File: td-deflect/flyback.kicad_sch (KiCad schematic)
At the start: 50 parts, among them Q12 G3R450MT17J, U13 MCP1416

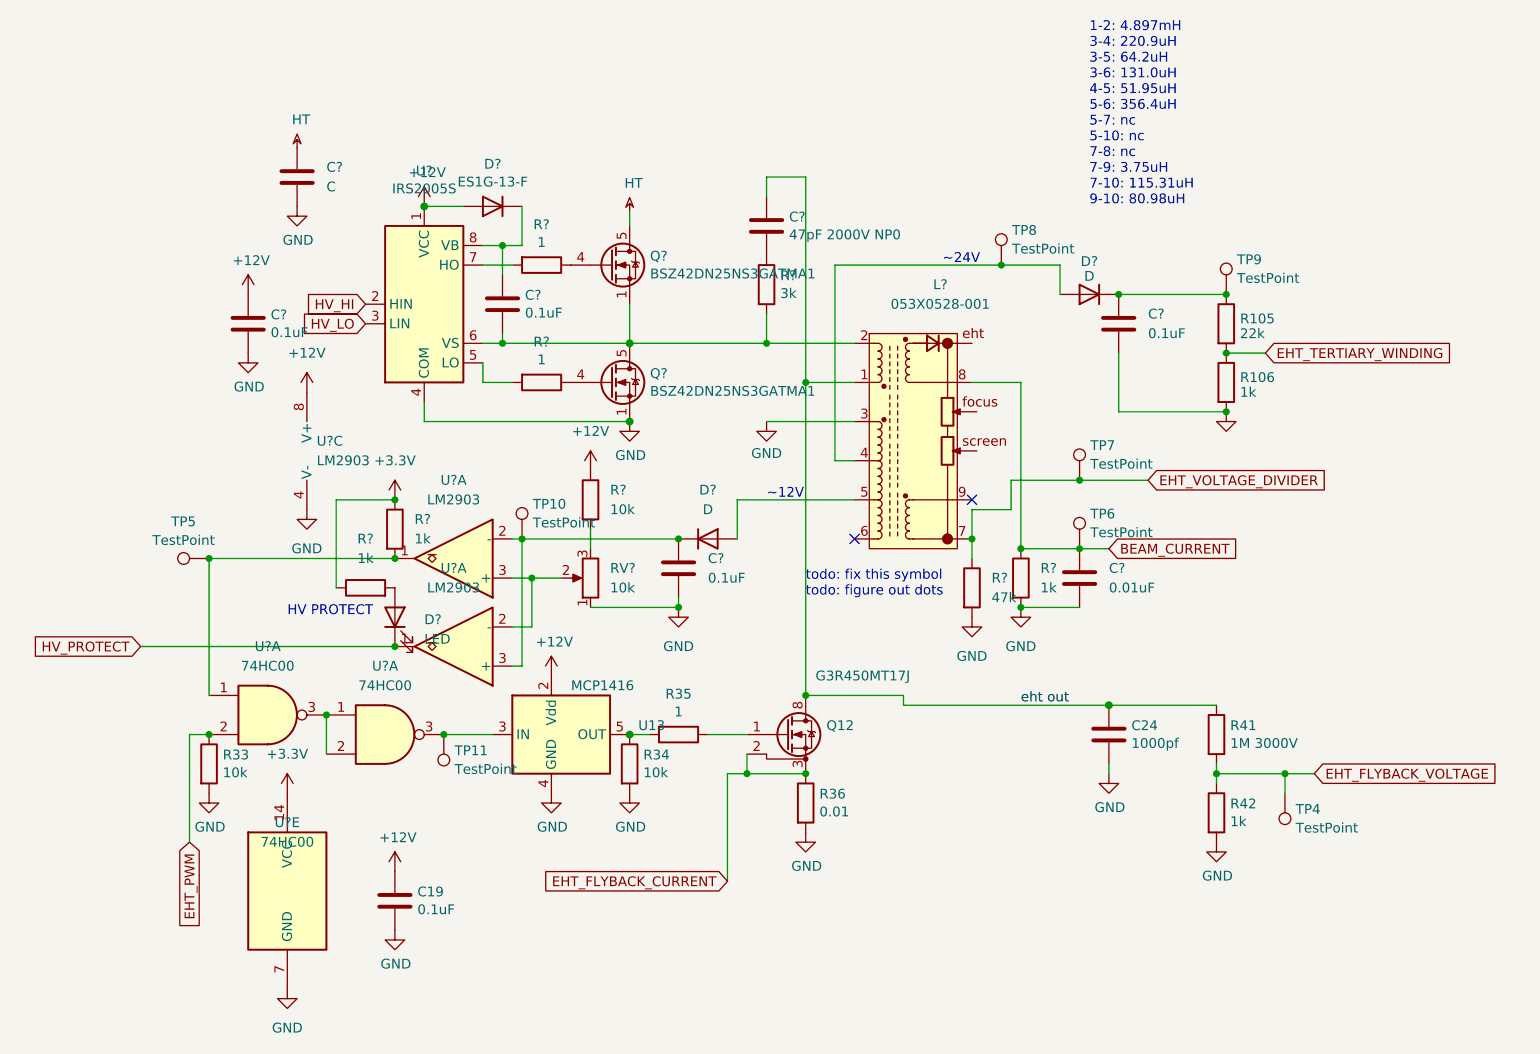
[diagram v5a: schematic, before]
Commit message: use offboard flyback
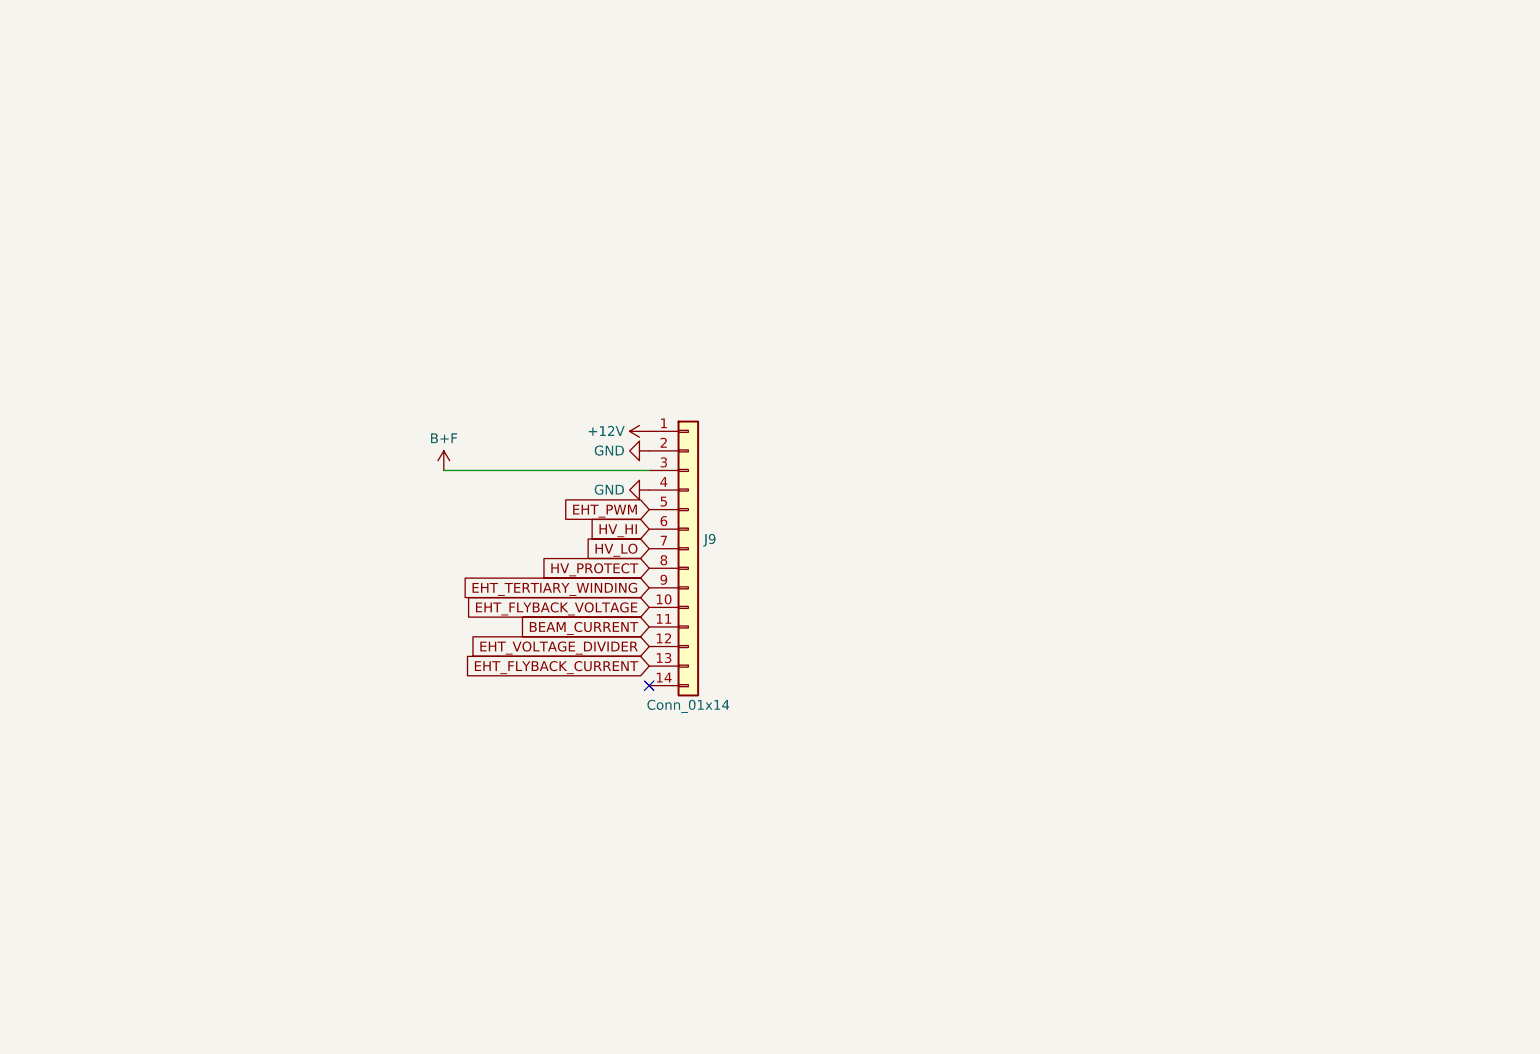
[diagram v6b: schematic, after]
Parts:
- removed C19, C? (x4): 0.1uF, Capacitor_SMD:C_0805_2012Metric_Pad1.18x1.45mm_HandSolder, symbol Device:C
- removed C24: 1000pf, Capacitor_THT:C_Rect_L18.0mm_W6.0mm_P15.00mm_FKS3_FKP3, symbol Device:C
- removed C?: 0.01uF, Capacitor_SMD:C_0805_2012Metric_Pad1.18x1.45mm_HandSolder, symbol Device:C
- removed C?: C, Capacitor_SMD:C_0805_2012Metric_Pad1.18x1.45mm_HandSolder, symbol Device:C
- removed C?: 47pF 2000V NP0, Capacitor_SMD:C_1206_3216Metric, symbol Device:C
- removed D? (x2): D, Diode_SMD:D_0805_2012Metric_Pad1.15x1.40mm_HandSolder, symbol Device:D
- removed D?: LED, Diode_SMD:D_0805_2012Metric_Pad1.15x1.40mm_HandSolder, symbol Device:LED
- removed D?: ES1G-13-F, Diode_SMD:D_SMA, symbol Diode:BA157
- removed L?: 053X0528-001, td-hv:053X0528-001, symbol td-hv:053X0528-001
- removed Q12: G3R450MT17J, Package_TO_SOT_SMD:TO-263-7_TabPin8, symbol Transistor_FET:C3M0280090J
- removed Q? (x2): BSZ42DN25NS3GATMA1, Package_TO_SOT_SMD:TDSON-8-1, symbol Transistor_FET:BSC082N10LSG
- removed R105: 22k, Resistor_SMD:R_0805_2012Metric_Pad1.20x1.40mm_HandSolder, symbol Device:R
- removed R106, R42, R? (x3): 1k, Resistor_SMD:R_0805_2012Metric_Pad1.20x1.40mm_HandSolder, symbol Device:R
- removed R33, R34, R?: 10k, Resistor_SMD:R_0805_2012Metric_Pad1.20x1.40mm_HandSolder, symbol Device:R
- removed R35, R? (x2): 1, Resistor_SMD:R_0805_2012Metric_Pad1.20x1.40mm_HandSolder, symbol Device:R
- removed R36: 0.01, Resistor_SMD:R_0805_2012Metric_Pad1.20x1.40mm_HandSolder, symbol Device:R
- removed R41: 1M 3000V, Resistor_SMD:R_2512_6332Metric, symbol Device:R
- removed R?: 47k, Resistor_SMD:R_0805_2012Metric_Pad1.20x1.40mm_HandSolder, symbol Device:R
- removed R?: 3k, Resistor_SMD:R_2512_6332Metric, symbol Device:R
- removed RV?: 10k, Potentiometer_THT:Potentiometer_Bourns_3386P_Vertical, symbol Device:R_Potentiometer
- removed TP10, TP11, TP4, TP5, TP6, TP7, TP8, TP9: TestPoint, TestPoint:TestPoint_Keystone_5010-5014_Multipurpose, symbol Connector:TestPoint
- removed U13: MCP1416, Package_TO_SOT_SMD:SOT-23-5, symbol Driver_FET:MCP1416
- removed U? (x3): LM2903, Package_SO:SOIC-8_3.9x4.9mm_P1.27mm, symbol Comparator:LM2903
- removed U? (x3): 74HC00, Package_SO:SOIC-14_3.9x8.7mm_P1.27mm, symbol 74xx:74HC00
- removed U?: IRS2005S, Package_SO:SOIC-8_3.9x4.9mm_P1.27mm, symbol Driver_FET:IRS2005S
- added J9: Conn_01x14, Connector_JST:JST_XH_B14B-XH-A_1x14_P2.50mm_Vertical, symbol Connector_Generic:Conn_01x14
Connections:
- net +12V: now also J9.1 (Pin_1)
- net +3.3V: now also J9.3 (Pin_3)
- net BEAM_CURRENT: now also J9.11 (Pin_11)
- net EHT_FLYBACK_CURRENT: now also J9.13 (Pin_13)
- net EHT_FLYBACK_VOLTAGE: now also J9.10 (Pin_10)
- net EHT_PWM: now also J9.5 (Pin_5)
- net EHT_TERTIARY_WINDING: now also J9.9 (Pin_9)
- net EHT_VOLTAGE_DIVIDER: now also J9.12 (Pin_12)
- net GND: now also J9.2 (Pin_2), J9.4 (Pin_4)
- net HV_HI: now also J9.6 (Pin_6)
- net HV_LO: now also J9.7 (Pin_7)
- net HV_PROTECT: now also J9.8 (Pin_8)
- no-connect marks 2 -> 1
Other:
- note removed: "1-2: 4.897mH 3-4: 220.9uH 3-5: 64.2uH 3-6: 131.0uH 4-5: 51.95uH 5-6: 356.4uH 5-7: nc 5-10: nc 7-8: nc 7-9: 3.75uH 7-10: 115.31uH 9-10: 80.98uH"
- note removed: "HV PROTECT"
- note removed: "todo: fix this symbol todo: figure out dots"
- note removed: "~12V"
- note removed: "~24V"

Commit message: fix remaining erc errors
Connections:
- net +3.3V renamed B+F
